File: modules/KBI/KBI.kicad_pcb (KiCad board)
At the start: 2 copper layers, 100 x 130 mm, 54 parts, among them IC1 Generic_OpAmp_Single_Swap, IC3 µA741C, IC4 µA741C, J1 +15V, J10 D, J11 E, J12 F, J13 G, J2 -15V, J3 GND, J4 KOV, J6 FM, J7 A, J8 B, J9 C, P1 1M, P2 100k, P3 100k, P4 100k, P5 100k, T1 N-FET, T2 N-FET, T3 N-FET, T4 N-FET

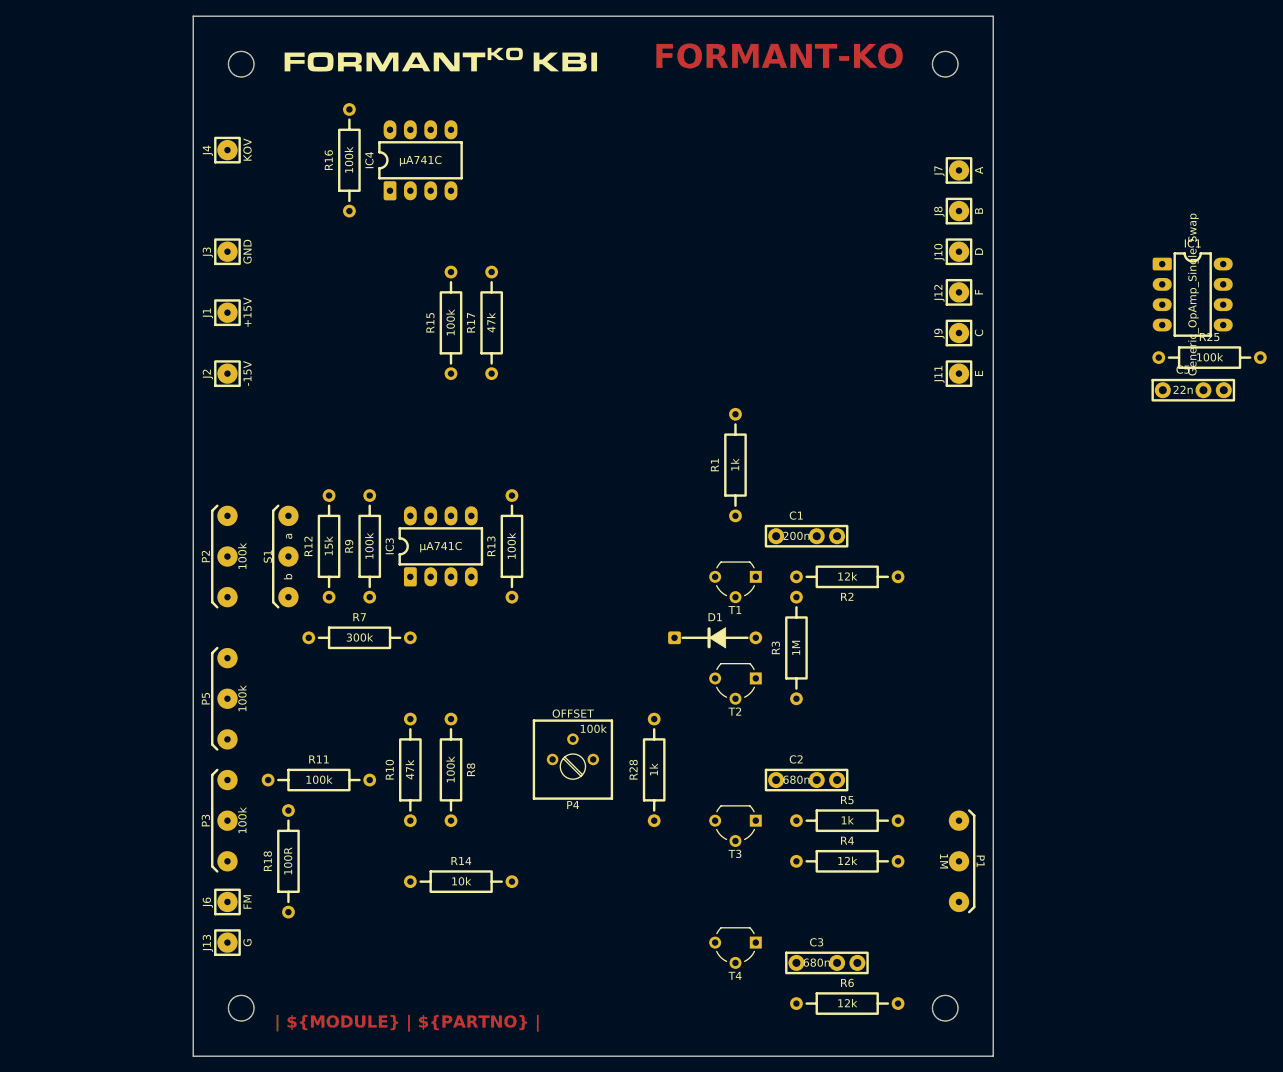
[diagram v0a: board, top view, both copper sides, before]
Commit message: added card extender to system
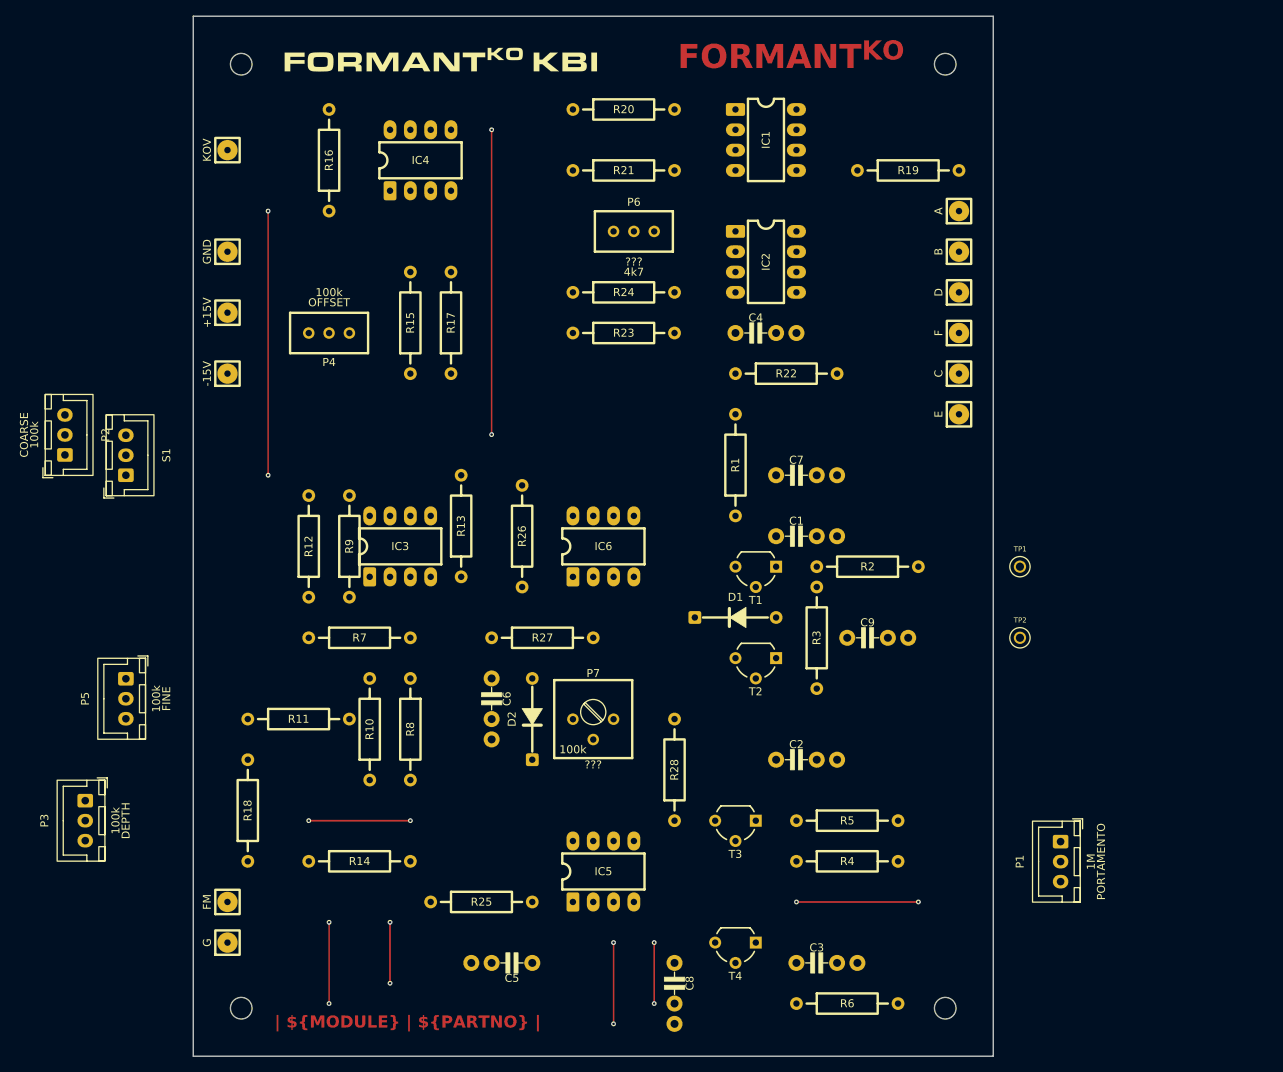
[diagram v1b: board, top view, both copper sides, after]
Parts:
- added C4: 1n, FormantKO:C_Rect, F.Cu at (161.9, 72.3)
- added C6: 220n, FormantKO:C_Rect, F.Cu at (128.9, 118.0)
- added C7: 680n, FormantKO:C_Rect, F.Cu at (167.0, 90.1)
- added C8: 680n, FormantKO:C_Rect, F.Cu at (151.8, 153.6)
- added C9: 680n, FormantKO:C_Rect, F.Cu at (175.9, 110.4)
- added D2: DUS, FormantKO:DUS, F.Cu at (134.0, 120.6)
- added IC1: OpAmp, FormantKO:DIP-8, F.Cu at (163.2, 48.2)
- added IC2: OpAmp, FormantKO:DIP-8, F.Cu at (163.2, 63.4)
- added IC6: Generic_OpAmp_Single_Swap, FormantKO:DIP-8, F.Cu at (142.9, 99.0)
- added P6: 4k7, FormantKO:Potentiometer_Trimmer_MultiTurn, F.Cu at (146.7, 59.6)
- added P7: 100k, FormantKO:Potentiometer_Trimmer, F.Cu at (141.6, 120.6)
- added R19: 1k, FormantKO:R_Axial_Horizontal, F.Cu at (181.0, 52.0)
- added R20: 10k, FormantKO:R_Axial_Horizontal, F.Cu at (145.4, 44.4)
- added R21: 4k7, FormantKO:R_Axial_Horizontal, F.Cu at (145.4, 52.0)
- added R22: 750R, FormantKO:R_Axial_Horizontal, F.Cu at (165.7, 77.4)
- added R23: 13k7, FormantKO:R_Axial_Horizontal, F.Cu at (145.4, 72.3)
- added R24: 1k, FormantKO:R_Axial_Horizontal, F.Cu at (145.4, 67.2)
- added R26: 12k, FormantKO:R_Axial_Horizontal, F.Cu at (132.7, 97.7)
- added R27: 2k2, FormantKO:R_Axial_Horizontal, F.Cu at (135.3, 110.4)
- added TP1: 2V3, FormantKO:KEYSTONE_5001, F.Cu at (194.9, 101.5)
- added TP2: 4V7, FormantKO:KEYSTONE_5001, F.Cu at (194.9, 110.4)
- C1, C2, C3, C5: footprint FormantKO:C_Disc -> FormantKO:C_Rect
- H1, H2, H3, H4: footprint FormantKO:MountingHole_3.2mm_M3 -> FormantKO:MountingHole_2.7mm_M2.5
- P1, P2, P3, P5: footprint FormantKO:Potentiometer_Inline -> FormantKO:PanelConnector_1x03
- P4: footprint FormantKO:Potentiometer_Trimmer -> FormantKO:Potentiometer_Trimmer_MultiTurn
- S1: footprint FormantKO:Switch_SPDT -> FormantKO:PanelConnector_1x03
- moved R25 113.6 mm to (127.6, 143.4)
- moved C5 110.3 mm to (131.4, 151.1), turned to 180 degrees
- moved IC5 103.1 mm to (142.9, 139.6), turned to 90 degrees
- moved P4 61.4 mm to (108.6, 72.3)
- moved P2 25.4 mm to (75.6, 85.1)
- moved S1 23.9 mm to (83.2, 87.6)
- moved P3 17.8 mm to (78.1, 133.3), turned to -90 degrees
- moved R14 13.0 mm to (112.4, 138.4)
- moved P1 12.7 mm to (200.0, 138.4)
- moved P5 12.7 mm to (83.2, 118.0), turned to -90 degrees
- moved R18 8.13 mm to (98.4, 132.0)
- moved R11 8.03 mm to (104.8, 120.6)
- moved R8 7.18 mm to (118.7, 121.9)
- moved R10 7.18 mm to (113.7, 121.9)
- moved R13 6.84 mm to (125.1, 96.5)
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- renumbered IC1 to IC5
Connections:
- C3 pad 1: unconnected-(C3-Pad1) -> Net-(T4-G)
- D1 pad 1: unconnected-(D1-K-Pad1) -> Net-(D1-K)
- IC5 pad 2: unconnected-(IC1---Pad2) -> Net-(D2-K)
- IC5 pad 6: unconnected-(IC1-Pad6) -> Net-(D2-K)
- P3 pad 1: unconnected-(P3-Pad1) -> FM
- R28 pad 1: unconnected-(R28-Pad1) -> Net-(D1-K)
- T4 pad 3: unconnected-(T4-D-Pad3) -> +15V
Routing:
- net (no net): track 0.00 -> 134.6 mm, vias 0 -> 16
